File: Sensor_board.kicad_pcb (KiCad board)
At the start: 2 copper layers, 100 x 100 mm, 91 parts, among them IC1 STM32G491CET6, J10 Conn_01x02, J11 Conn_01x02, J12 Conn_01x02, J13 Conn_01x04, J14 Conn_01x04, J15 Conn_01x06, J16 Conn_01x06, J17 Conn_02x08_Odd_Even, J18 Conn_01x03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

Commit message: 60% of trace
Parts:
- removed D4: VCC_OK, LED_SMD:LED_0805_2012Metric_Pad1.15x1.40mm_HandSolder
- removed D5: 5V_OK, LED_SMD:LED_0805_2012Metric_Pad1.15x1.40mm_HandSolder
- removed D6: 3V3_OK, LED_SMD:LED_0805_2012Metric_Pad1.15x1.40mm_HandSolder
- removed J23: Conn_01x04, easyeda2kicad:CONN-TH_4P-XT30PW-M
- removed R18: 22k, Resistor_SMD:R_0603_1608Metric_Pad0.98x0.95mm_HandSolder
- removed R19, R20: 1k, Resistor_SMD:R_0603_1608Metric_Pad0.98x0.95mm_HandSolder
- J24: moved to F.Cu
- moved C25 5.23 mm to (138.1, 73.8)
- moved J24 1.70 mm to (180.4, 45.2), turned to 90 degrees
- moved C2 0.89 mm to (97.3, 79.9)
- moved C4 0.89 mm to (97.3, 82.4)
- moved D1 0.89 mm to (97.0, 88.7)
- moved TP5 0.89 mm to (106.0, 82.1)
- moved U4 0.89 mm to (116.3, 89.5)
- moved C16 0.89 mm to (119.8, 83.6)
- moved C5 0.89 mm to (97.3, 84.9)
- moved C6 0.89 mm to (99.1, 87.9)
- moved C7 0.89 mm to (104.6, 87.9)
- moved JP4 0.89 mm to (114.2, 81.3)
- moved U2 0.89 mm to (102.1, 88.8)
- moved C11 0.89 mm to (108.1, 81.2)
- moved C12 0.89 mm to (110.1, 81.2)
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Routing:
- net /BATT: track 18.7 -> 108.1 mm
- net GND: track 43.7 -> 132.0 mm
- net /NRST: track 71.8 -> 34.8 mm, vias 4 -> 0
- net /PB5: track 42.4 -> 31.4 mm, vias 0 -> 2
- net +3.3V: track 35.1 -> 45.6 mm
- net /TIM2_CH4: track 17.8 -> 25.0 mm, vias 1 -> 3
- net Net-(U2-FB): track 9.23 -> 12.3 mm

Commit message: almost done
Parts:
- removed H1, H2, H3, H4: MountingHole_Pad, MountingHole:MountingHole_3.2mm_M3_DIN965_Pad
- removed J10, J11, J12, J3, J8: Conn_01x02, Connector_Molex:Molex_SPOX_5267-02A_1x02_P2.50mm_Vertical
- added H5: MountingHole, MountingHole:MountingHole_3.2mm_M3_ISO7380, F.Cu at (186.0, 126.0)
- added H6: MountingHole, MountingHole:MountingHole_3.2mm_M3_ISO7380, F.Cu at (186.0, 34.0)
- added H7: MountingHole, MountingHole:MountingHole_3.2mm_M3_ISO7380, F.Cu at (94.0, 34.0)
- added H8: MountingHole, MountingHole:MountingHole_3.2mm_M3_ISO7380, F.Cu at (94.0, 126.0)
- JP4: footprint Jumper:SolderJumper-2_P1.3mm_Open_RoundedPad1.0x1.5mm -> Jumper:SolderJumper-2_P1.3mm_Open_TrianglePad1.0x1.5mm
- moved R14 106.2 mm to (141.9, 80.1), turned to 180 degrees
- moved R8 104.0 mm to (127.6, 98.0), turned to 180 degrees
- moved D3 103.4 mm to (141.9, 77.8), turned to 180 degrees
- moved R13 100.8 mm to (146.9, 80.1)
- moved D2 97.7 mm to (146.9, 77.8)
- moved SW2 93.4 mm to (128.4, 102.0), turned to -90 degrees
- moved J14 24.9 mm to (148.1, 112.0)
- moved J13 24.7 mm to (148.1, 102.0)
- moved R9 17.8 mm to (150.4, 94.4)
- moved R6 15.9 mm to (150.4, 92.7)
- moved R7 13.9 mm to (150.4, 105.4)
- moved R10 13.8 mm to (150.4, 107.2)
- moved J22 4.00 mm to (175.9, 112.0)
- moved R1 3.59 mm to (144.2, 43.6)
- moved C16 3.58 mm to (122.3, 86.2)
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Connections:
- J17 pad 2: +3.3V -> +5V
- J17 pad 4: +5V -> +3.3V
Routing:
- net +3.3V: track 45.6 -> 401.5 mm, vias 0 -> 7
- net +5V: track 5.34 -> 145.3 mm, vias 0 -> 4
- net /CAN_1_H: track 4.48 -> 136.4 mm
- net /CAN_1_L: track 4.48 -> 131.2 mm
- net GND: track 132.0 -> 185.6 mm, vias 2 -> 37
- net /BATT: track 108.1 -> 160.5 mm
- net /PC13: track 31.3 -> 74.5 mm, vias 1 -> 4
- net /PA4: track 102.2 -> 63.8 mm, vias 1 -> 0
- net /PA6: track 89.5 -> 59.3 mm, vias 2 -> 3
- net /I2C2_SDA: track 70.9 -> 92.0 mm, vias 1 -> 2
- net /I2C2_SCL: track 72.2 -> 90.9 mm, vias 1 -> 2
- net /PB9: track 64.0 -> 46.6 mm
- net /PB2: track 46.5 -> 29.7 mm, vias 2 -> 0
- net /SWCLK: track 44.7 -> 28.2 mm, vias 3 -> 1
- net /I2C1_SDA: track 43.0 -> 58.9 mm, vias 1 -> 2
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- added copper zone on B.Cu, net GND
- added copper zone on F.Cu, net GND
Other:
- outline, holes or cut-outs redrawn
- board text added: "1 2 3"
- board text added: "JP2"
- board text added: "JP3"
- board text removed: "3 2 1"

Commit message: Ready for review from Mr Kettle
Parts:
- added C1: 22uF, Capacitor_THT:CP_Radial_D5.0mm_P2.00mm, F.Cu at (112.0, 117.0)
- added C2: 220uF, Capacitor_THT:CP_Radial_D6.3mm_P2.50mm, F.Cu at (112.9, 110.1)
- added D1: D_Schottky, Diode_SMD:D_SMA, B.Cu at (103.4, 114.3)
- added H1: MountingHole, MountingHole:MountingHole_3.2mm_M3_DIN965_Pad_TopBottom, F.Cu at (104.4, 121.1)
- added H2: MountingHole, MountingHole:MountingHole_3.2mm_M3_DIN965_Pad_TopBottom, F.Cu at (114.6, 103.6)
- added J1: IN, Connector_PinSocket_2.54mm:PinSocket_1x02_P2.54mm_Vertical, F.Cu at (112.0, 121.0)
- added J2: OUT, Connector_PinSocket_2.54mm:PinSocket_1x02_P2.54mm_Vertical, F.Cu at (108.0, 102.2)
- added L1: 330 uH, Inductor_THT:L_Radial_D8.7mm_P5.00mm_Fastron_07HCP, F.Cu at (103.8, 109.7)
- added U1: LM2574HVM-5, Package_SO:SOIC-14W_7.5x9mm_P1.27mm, B.Cu at (111.3, 113.3)
- added mouse-bite-2mm-slot: VAL**, Panelization:mouse-bite-2mm-slot, F.Cu at (109.6, 125.2)
- added mouse-bite-2mm-slot: VAL**, Panelization:mouse-bite-2mm-slot, F.Cu at (100.4, 114.8)
- added mouse-bite-2mm-slot: VAL**, Panelization:mouse-bite-2mm-slot, F.Cu at (118.6, 118.0)
- added mouse-bite-2mm-slot: VAL**, Panelization:mouse-bite-2mm-slot, F.Cu at (110.2, 99.5)
- added mouse-bite-2mm-slot: VAL**, Panelization:mouse-bite-2mm-slot, F.Cu at (118.6, 107.9)
- added mouse-bite-2mm-slot: VAL**, Panelization:mouse-bite-2mm-slot, F.Cu at (100.4, 106.4)
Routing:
- net (no net): track 0.00 -> 29.7 mm
- net Net-(D1-K): track 6.34 -> 12.2 mm
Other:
- outline, holes or cut-outs redrawn
- board text added: "3V3"
- board text added: "50V"
- board text added: "Extra step-down xD"
- board text added: "GND"
- board text added: "J9 <pinout>"
- board text added: "NRST"
- board text added: "SWCLK"
- board text added: "SWDIO"
- board text added: "UART1"

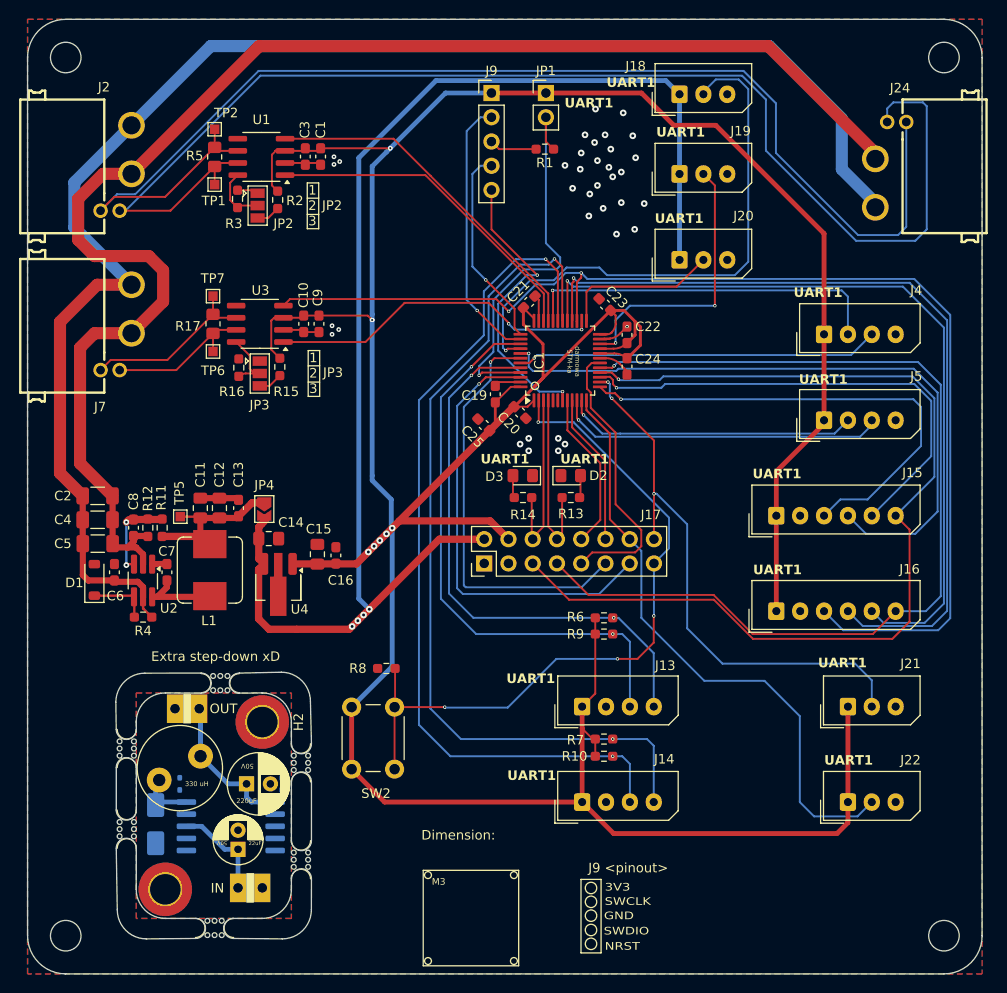
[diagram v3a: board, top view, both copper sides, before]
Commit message: Updated silkscreen
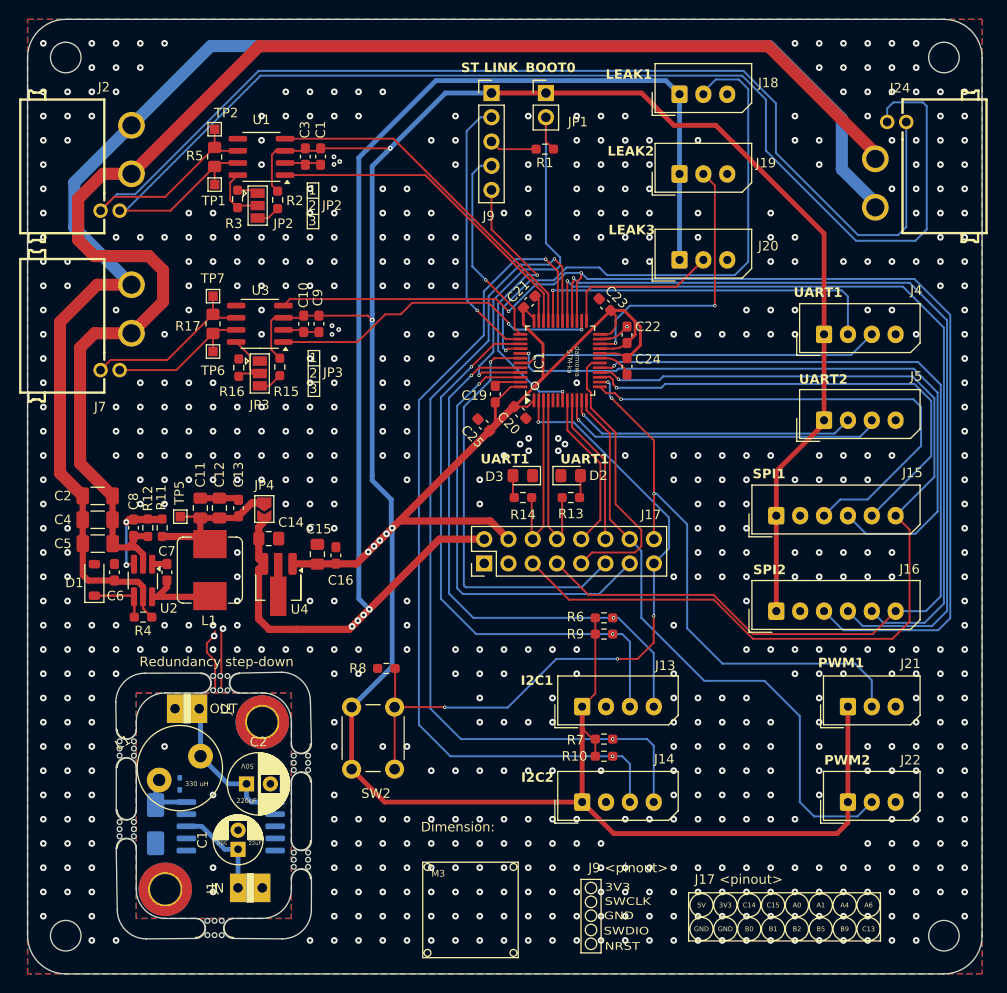
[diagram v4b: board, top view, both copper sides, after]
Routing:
- net (no net): track 29.7 -> 43.1 mm, vias 0 -> 2
- net GND: vias 37 -> 662
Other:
- board text added: "5V"
- board text added: "A0"
- board text added: "A1"
- board text added: "A4"
- board text added: "A6"
- board text added: "B0"
- board text added: "B1"
- board text added: "B2"
- board text added: "B5"
- board text added: "B9"
- board text added: "BOOT0"
- board text added: "C13"
- board text added: "C14"
- board text added: "C15"
- board text added: "I2C1"
- board text added: "I2C2"
- board text added: "J17 <pinout>"
- board text added: "LEAK1"
- board text added: "LEAK2"
- board text added: "LEAK3"
- board text added: "PWM1"
- board text added: "PWM2"
- board text added: "Redundancy step-down"
- board text added: "SPI1"
- board text added: "SPI2"
- board text added: "ST LINK"
- board text added: "UART2"
- board text removed: "Extra step-down xD"

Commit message: major route chanses to improve overall layout
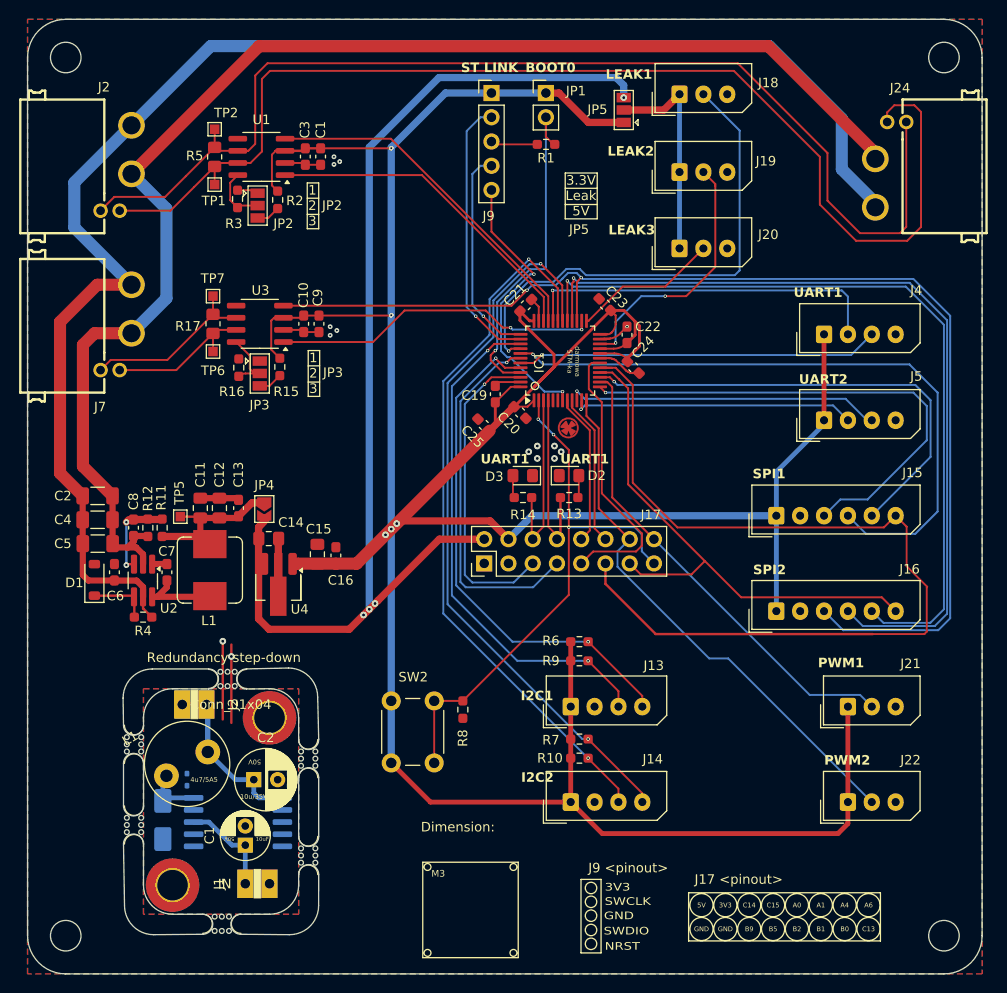
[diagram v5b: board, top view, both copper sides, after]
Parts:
- removed the mouse-bite-2mm-slot at (109.6, 125.2)
- removed the mouse-bite-2mm-slot at (100.4, 114.8)
- removed the mouse-bite-2mm-slot at (118.6, 118.0)
- removed the mouse-bite-2mm-slot at (110.2, 99.5)
- removed the mouse-bite-2mm-slot at (118.6, 107.9)
- removed the mouse-bite-2mm-slot at (100.4, 106.4)
- added JP5: SolderJumper_3_Open, Jumper:SolderJumper-3_P1.3mm_Open_Pad1.0x1.5mm, F.Cu at (152.5, 39.5)
- added mouse-bite-2mm-slot: VAL**, Panelization:mouse-bite-2mm-slot, F.Cu at (119.4, 117.6)
- added mouse-bite-2mm-slot: VAL**, Panelization:mouse-bite-2mm-slot, F.Cu at (111.0, 99.1)
- added mouse-bite-2mm-slot: VAL**, Panelization:mouse-bite-2mm-slot, F.Cu at (110.3, 124.8)
- added mouse-bite-2mm-slot: VAL**, Panelization:mouse-bite-2mm-slot, F.Cu at (119.4, 107.5)
- added mouse-bite-2mm-slot: VAL**, Panelization:mouse-bite-2mm-slot, F.Cu at (101.2, 114.4)
- added mouse-bite-2mm-slot: VAL**, Panelization:mouse-bite-2mm-slot, F.Cu at (101.2, 106.0)
- C1: value 22uF -> 10uF
- C2: value 220uF -> 10u/35V
- D1: value D_Schottky -> 5V
- J2: value OUT -> Conn_01x04
- L1: value 330 uH -> 4u7/5A5
- U1: value LM2574HVM-5 -> SN65HVD230
- moved R8 9.10 mm to (135.6, 102.3), turned to -90 degrees
- moved SW2 4.20 mm to (132.6, 101.4)
- moved R9 3.80 mm to (147.8, 97.2)
- moved R6 3.59 mm to (147.8, 95.2)
- moved R10 2.58 mm to (147.8, 107.4)
- moved R7 2.57 mm to (147.8, 105.4)
- moved J20 1.20 mm to (158.3, 54.0)
- moved J13 1.20 mm to (146.9, 102.0)
- moved J14 1.20 mm to (146.9, 112.0)
- moved C1 0.88 mm to (112.8, 116.5)
- moved J1 0.88 mm to (112.8, 120.5)
- moved C2 0.88 mm to (113.7, 109.7)
- moved D1 0.88 mm to (104.2, 113.9)
- moved U1 0.88 mm to (112.0, 112.8)
- moved H1 0.88 mm to (105.2, 120.7)
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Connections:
- C1 pad 1: (no net) -> +3.3V
- C2 pad 1: (no net) -> /BATT
- J15 pad 6: /PB0 -> /PB1
- J16 pad 6: /PB1 -> /PB0
- J17 pad 11: /PB5 -> /PB1
- J17 pad 13: /PB9 -> /PB0
- J17 pad 5: /PB0 -> /PB9
- J17 pad 7: /PB1 -> /PB5
- J18 pad 1: +5V -> Net-(J18-Pin_1)
- J19 pad 1: +5V -> Net-(J18-Pin_1)
- J2 pad 1: (no net) -> /BATT
- J20 pad 1: +5V -> unconnected-(J20-Pin_1-Pad1)
- L1 pad 1: Net-(D1-K) -> Net-(U2-LX)
- L1 pad 2: (no net) -> Net-(JP4-A)
- U1 pad 1: (no net) -> /FDCAN1_TX
- U1 pad 12: Net-(D1-K) -> (no net)
- U1 pad 2: (no net) -> GND
- U1 pad 3: (no net) -> +3.3V
- U1 pad 4: GND -> /FDCAN1_RX
- U1 pad 5: GND -> unconnected-(U1-Vref-Pad5)
- U1 pad 6: GND -> /CAN_1_L
- U1 pad 7: (no net) -> /CAN_1_H
- U1 pad 8: (no net) -> Net-(JP2-C)
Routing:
- net /PB0: track 105.7 -> 56.1 mm, vias 1 -> 0
- net (no net): track 43.1 -> 19.6 mm, vias 2 -> 0
- net +3.3V: track 401.5 -> 378.0 mm, vias 7 -> 5
- net /PC13: track 74.5 -> 58.5 mm, vias 4 -> 3
- net /I2C2_SDA: track 92.0 -> 76.8 mm
- net /I2C2_SCL: track 90.9 -> 75.9 mm
- net /PB9: track 46.6 -> 33.2 mm
- net /CAN_1_L: track 131.2 -> 118.8 mm
- net /CAN_1_H: track 136.4 -> 125.1 mm
- net /PA6: track 59.3 -> 49.3 mm, vias 3 -> 0
- net +5V: track 145.3 -> 153.6 mm, vias 4 -> 6
- net /PA4: track 63.8 -> 56.7 mm
- net Net-(J18-Pin_1): track 0.00 -> 6.53 mm
- net GND: track 185.6 -> 179.5 mm, vias 662 -> 13
- net /I2C1_SCL: track 60.2 -> 54.2 mm
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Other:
- outline, holes or cut-outs redrawn
- board text added: "3.3V Leak 5V"
- board text added: "JP5"

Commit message: final design version
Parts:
- added D7: ~, LED_SMD:LED_0805_2012Metric_Pad1.15x1.40mm_HandSolder, F.Cu at (129.1, 95.3)
- added D8: ~, LED_SMD:LED_0805_2012Metric_Pad1.15x1.40mm_HandSolder, F.Cu at (129.1, 76.8)
- added R21: 1k, Resistor_SMD:R_0603_1608Metric_Pad0.98x0.95mm_HandSolder, F.Cu at (128.1, 92.3)
- added R22: 120, Resistor_SMD:R_0603_1608Metric_Pad0.98x0.95mm_HandSolder, F.Cu at (128.1, 80.1)
- added REF**: TestPoint_Pad_D1.0mm, TestPoint:TestPoint_Pad_D1.0mm, F.Cu at (145.8, 72.5)
- H1, H2: footprint MountingHole:MountingHole_3.2mm_M3_DIN965_Pad_TopBottom -> MountingHole:MountingHole_3.2mm_M3_ISO7380
- H5, H6, H7, H8: footprint MountingHole:MountingHole_3.2mm_M3_ISO7380 -> MountingHole:MountingHole_3.2mm_M3_ISO7380_Pad
- moved C9 1.97 mm to (122.5, 61.9)
- moved C1 1.80 mm to (122.5, 44.4)
- moved C10 1.07 mm to (120.0, 61.9)
- moved R17 0.93 mm to (108.5, 61.9)
- moved C3 0.90 mm to (120.0, 44.4)
- moved R3 0.85 mm to (111.5, 49.5)
- moved R15 0.68 mm to (116.4, 67.1)
- moved R2 0.66 mm to (116.5, 49.5)
- moved TP7 0.64 mm to (108.8, 58.9)
- moved R16 0.60 mm to (112.1, 67.1)
- moved R5 0.60 mm to (109.0, 44.4)
- moved TP1 0.53 mm to (109.2, 47.6)
- moved TP2 0.51 mm to (109.1, 41.4)
- moved TP6 0.36 mm to (109.1, 65.0)
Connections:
- J20 pad 1: unconnected-(J20-Pin_1-Pad1) -> Net-(J18-Pin_1)
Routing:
- net Net-(J18-Pin_1): track 6.53 -> 22.7 mm
- net +5V: track 153.6 -> 139.3 mm
- net +3.3V: track 378.0 -> 385.4 mm, vias 5 -> 9
- net RCC_OSC_OUT: track 0.00 -> 4.14 mm
- net /RCC_OSC_IN: track 0.00 -> 2.75 mm
- net /SPI2_MISO: track 87.8 -> 90.4 mm
- net GND: track 179.5 -> 182.0 mm, vias 13 -> 833
- net Net-(D8-A): track 0.00 -> 2.30 mm
- net /FDCAN2_RX: track 124.2 -> 126.2 mm
- net Net-(D7-A): track 0.00 -> 2.08 mm
- net Net-(JP2-C): track 6.25 -> 8.11 mm
- net Net-(JP3-C): track 6.92 -> 8.22 mm
- net /TIM2_CH2: track 53.2 -> 54.3 mm
- net /I2C2_SCL: track 75.9 -> 76.6 mm
- net /SPI1_SCK: track 52.7 -> 52.0 mm
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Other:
- board text added: "5V Leak 3.3V"
- board text added: "Sensor Board: Mikołaj Czerniak Damian Kociołek KN Robocik 2024/25"
- board text removed: "3.3V Leak 5V"
